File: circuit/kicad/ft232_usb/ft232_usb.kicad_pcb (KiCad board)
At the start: 2 copper layers, 40.4 x 24.4 mm, 19 parts, among them J1 Conn_01x03_Male, J2 Conn_01x05_Male, J3 USB_B_Micro, U1 FT232RL

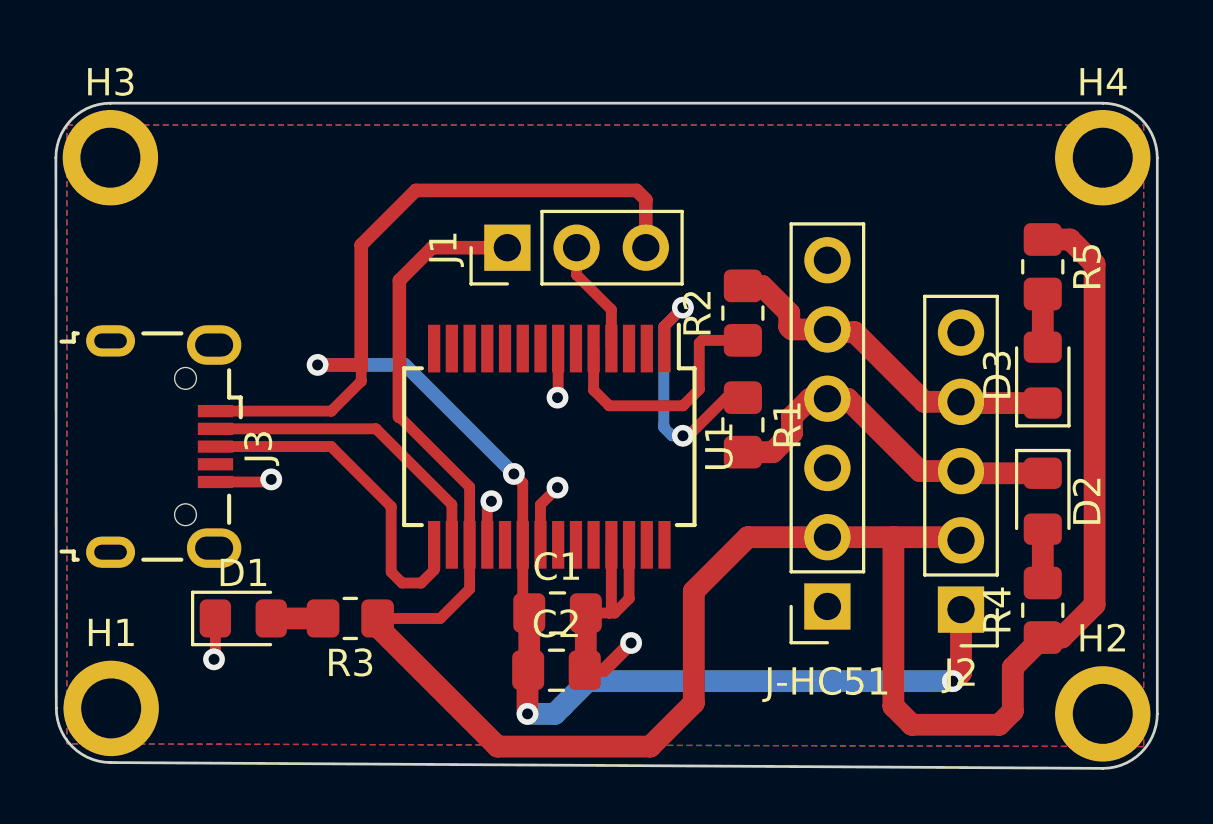
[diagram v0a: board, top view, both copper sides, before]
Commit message: Migrate Eagle-KiCAD
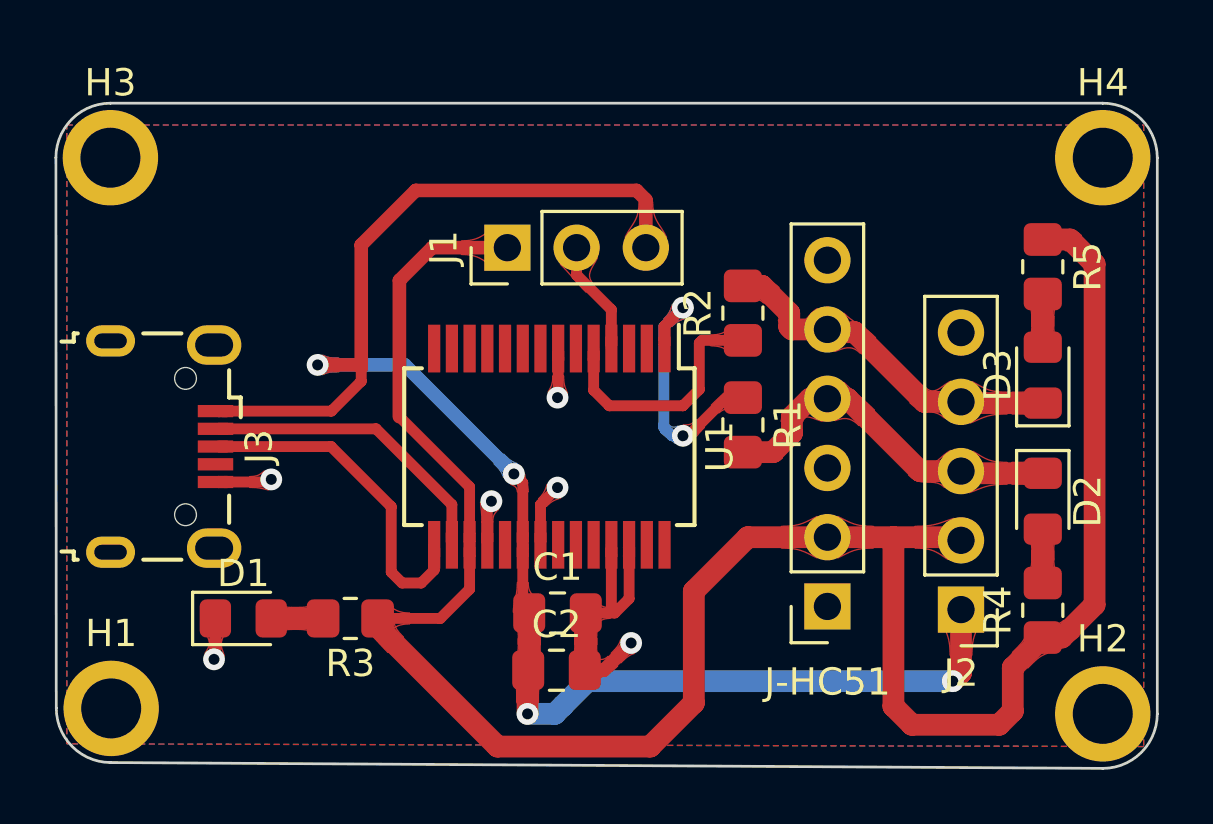
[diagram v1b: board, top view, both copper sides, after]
